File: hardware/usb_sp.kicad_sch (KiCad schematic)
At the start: 0 parts

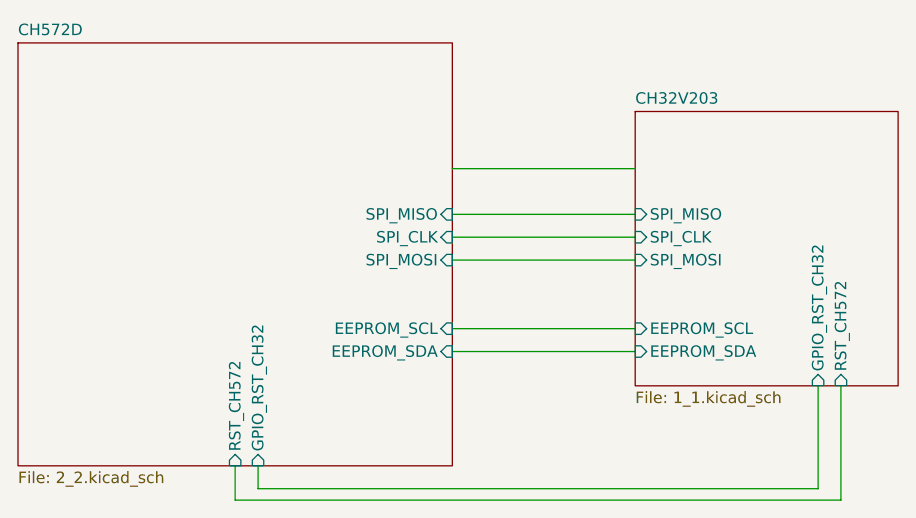
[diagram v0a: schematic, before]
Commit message: fix: add missing cs line to spi bus
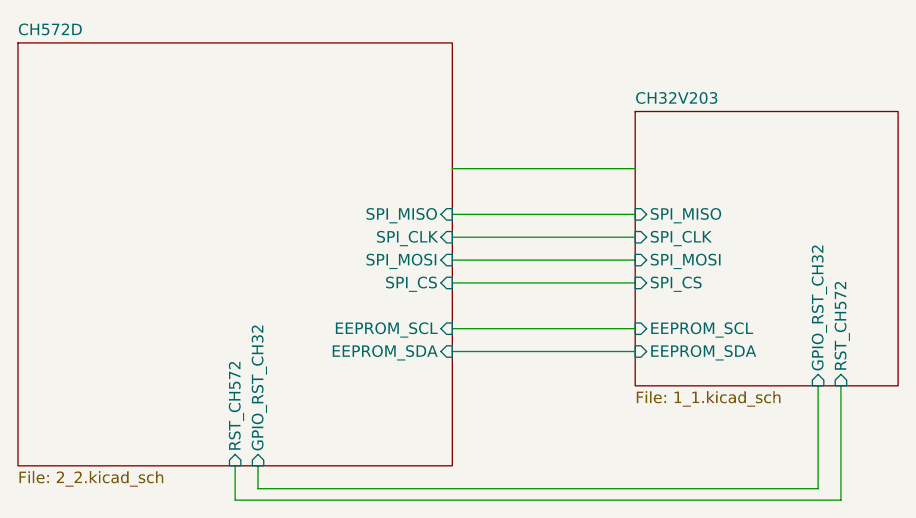
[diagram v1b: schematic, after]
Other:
- sheet CH32V203 ports: added SPI_CS; removed none
- sheet CH572D ports: added SPI_CS; removed none
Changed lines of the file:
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@@
+	(wire
+		(pts
+			(xy 102.87 68.58) (xy 123.19 68.58)
+		)
+		(stroke
+			(width 0)
+			(type default)
+		)
+	)
 	(wire
 		(pts
@@
 			)
 		)
+		(pin "SPI_CS" input
+			(at 123.19 68.58 180)
+			(effects
+				(font
+					(size 1.27 1.27)
+				)
+				(justify left)
+			)
+		)
 		(instances
 			(project "usb_sp"
@@
 			)
 		)
+		(pin "SPI_CS" input
+			(at 102.87 68.58 0)
+			(effects
+				(font
+					(size 1.27 1.27)
+				)
+				(justify right)
+			)
+		)
